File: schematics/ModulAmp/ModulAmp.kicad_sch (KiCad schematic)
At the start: 0 parts

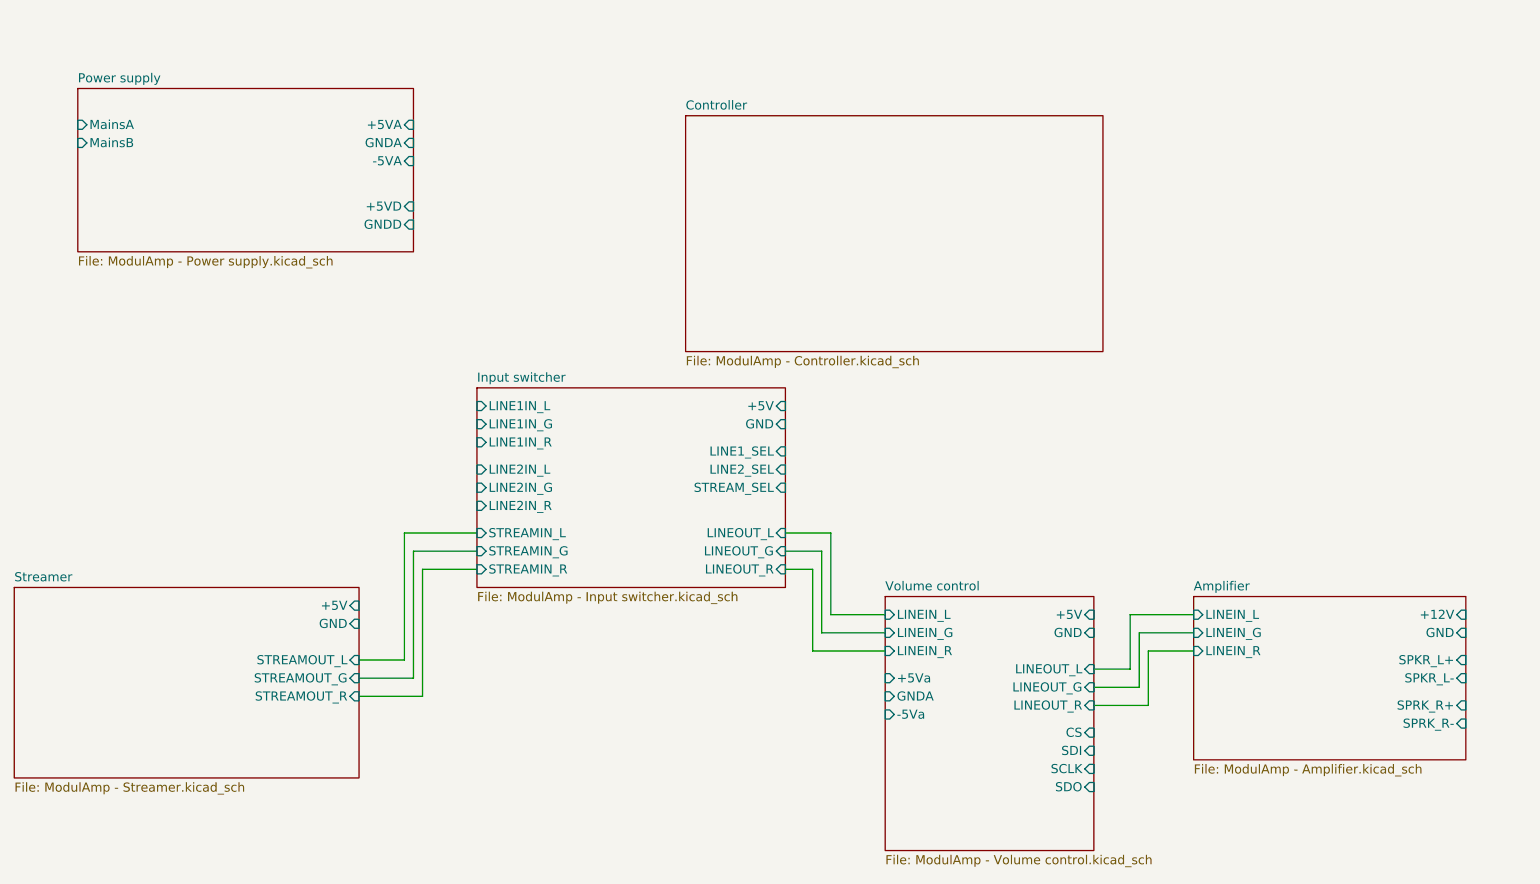
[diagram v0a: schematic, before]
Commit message: Refactored strings and added DHTxx full support
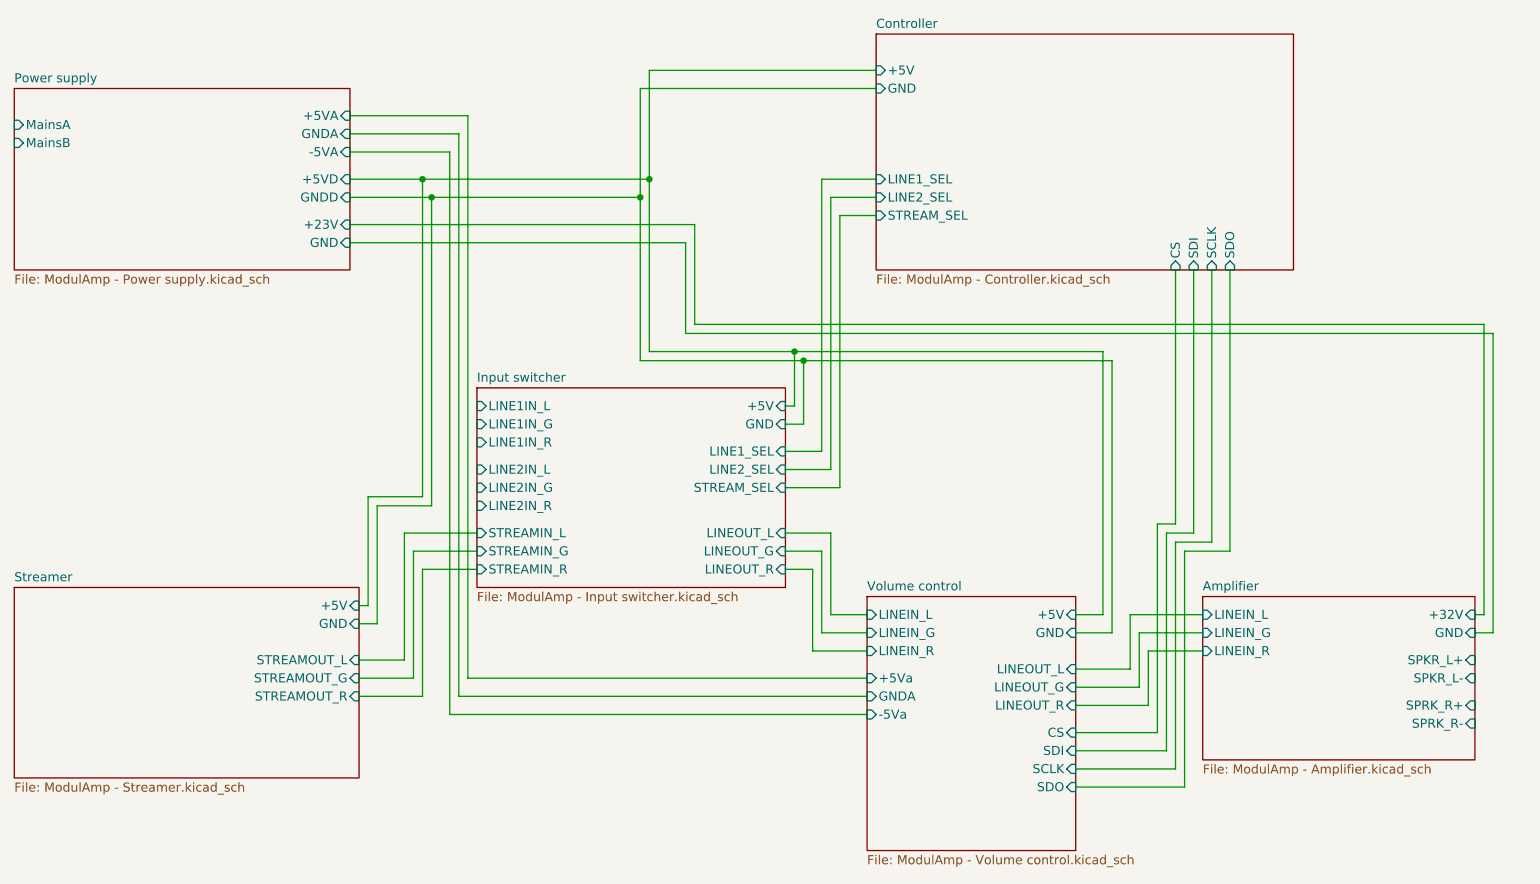
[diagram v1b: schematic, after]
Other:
- sheet Amplifier ports: added +32V; removed +12V
- sheet Controller ports: added +5V, CS, GND, LINE1_SEL, LINE2_SEL, SCLK, SDI, SDO, STREAM_SEL; removed none
- sheet Power supply ports: added +23V, GND; removed none
